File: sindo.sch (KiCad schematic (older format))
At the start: 153 parts, among them J1 Conn_02x06_Odd_Even, J2 Conn_02x06_Odd_Even, U1 ESP32DEVKITV1

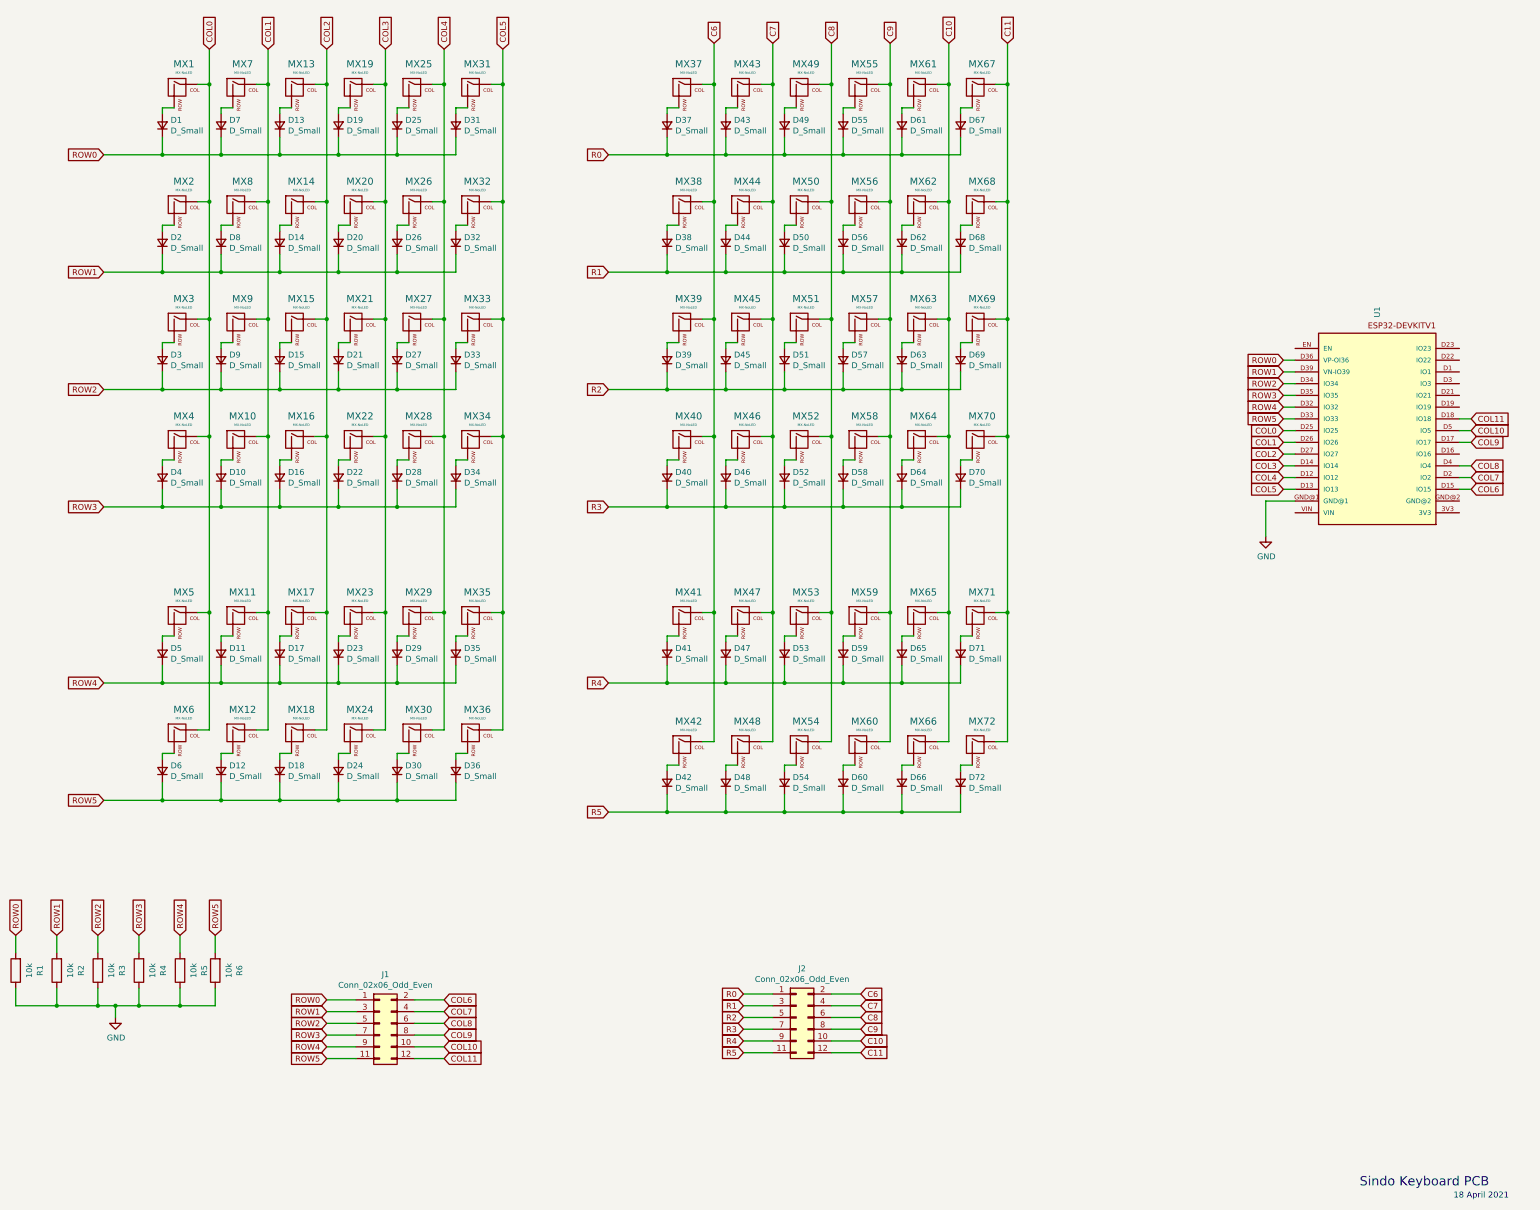
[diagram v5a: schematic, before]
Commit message: Reworked the layout for a single layer
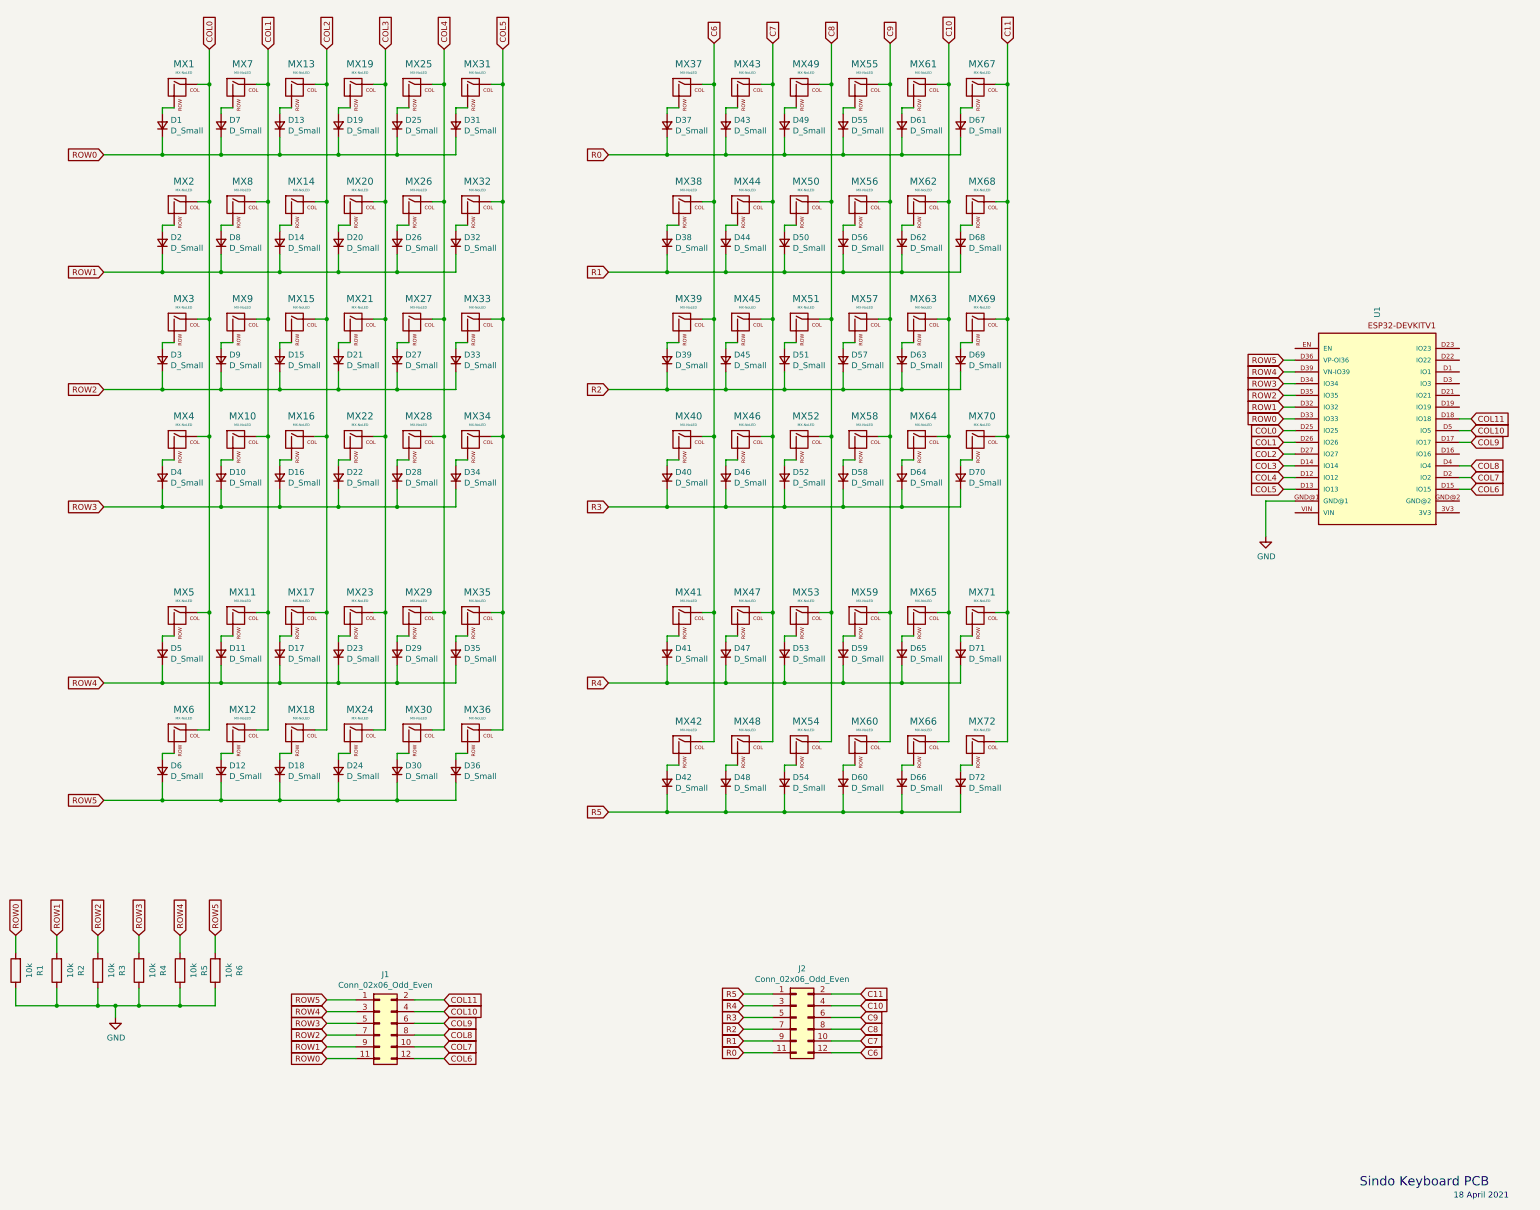
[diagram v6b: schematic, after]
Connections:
- net C10: now also J2.4 (Pin_4); no longer J2.10 (Pin_10)
- net C11: now also J2.2 (Pin_2); no longer J2.12 (Pin_12)
- net C6: now also J2.12 (Pin_12); no longer J2.2 (Pin_2)
- net C7: now also J2.10 (Pin_10); no longer J2.4 (Pin_4)
- net C8: now also J2.8 (Pin_8); no longer J2.6 (Pin_6)
- net C9: now also J2.6 (Pin_6); no longer J2.8 (Pin_8)
- net COL10: now also J1.4 (Pin_4); no longer J1.10 (Pin_10)
- net COL11: now also J1.2 (Pin_2); no longer J1.12 (Pin_12)
- net COL6: now also J1.12 (Pin_12); no longer J1.2 (Pin_2)
- net COL7: now also J1.10 (Pin_10); no longer J1.4 (Pin_4)
- net COL8: now also J1.8 (Pin_8); no longer J1.6 (Pin_6)
- net COL9: now also J1.6 (Pin_6); no longer J1.8 (Pin_8)
- net R0: now also J2.11 (Pin_11); no longer J2.1 (Pin_1)
- net R1: now also J2.9 (Pin_9); no longer J2.3 (Pin_3)
- net R2: now also J2.7 (Pin_7); no longer J2.5 (Pin_5)
- net R3: now also J2.5 (Pin_5); no longer J2.7 (Pin_7)
- net R4: now also J2.3 (Pin_3); no longer J2.9 (Pin_9)
- net R5: now also J2.1 (Pin_1); no longer J2.11 (Pin_11)
- net ROW0: now also J1.11 (Pin_11), U1.D33 (IO33); no longer J1.1 (Pin_1), U1.D36 (VP-OI36)
- net ROW1: now also J1.9 (Pin_9), U1.D32 (IO32); no longer J1.3 (Pin_3), U1.D39 (VN-IO39)
- net ROW2: now also J1.7 (Pin_7), U1.D35 (IO35); no longer J1.5 (Pin_5), U1.D34 (IO34)
- net ROW3: now also J1.5 (Pin_5), U1.D34 (IO34); no longer J1.7 (Pin_7), U1.D35 (IO35)
- net ROW4: now also J1.3 (Pin_3), U1.D39 (VN-IO39); no longer J1.9 (Pin_9), U1.D32 (IO32)
- net ROW5: now also J1.1 (Pin_1), U1.D36 (VP-OI36); no longer J1.11 (Pin_11), U1.D33 (IO33)
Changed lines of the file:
@@
 Text GLabel 4900 1250 1    50   Input ~ 0
 COL5
+Text GLabel 3400 9850 0    50   Input ~ 0
+ROW0
+Text GLabel 3400 9650 0    50   Input ~ 0
+ROW2
+Text GLabel 3400 9550 0    50   Input ~ 0
+ROW3
+Text GLabel 3400 9450 0    50   Input ~ 0
+ROW4
 Text GLabel 3400 9350 0    50   Input ~ 0
-ROW0
-Text GLabel 3400 9450 0    50   Input ~ 0
-ROW1
-Text GLabel 3400 9550 0    50   Input ~ 0
-ROW2
-Text GLabel 3400 9650 0    50   Input ~ 0
-ROW3
-Text GLabel 3400 9750 0    50   Input ~ 0
-ROW4
-Text GLabel 3400 9850 0    50   Input ~ 0
 ROW5
+Text GLabel 4400 9850 2    50   Input ~ 0
+COL6
+Text GLabel 4400 9750 2    50   Input ~ 0
+COL7
+Text GLabel 4400 9650 2    50   Input ~ 0
+COL8
+Text GLabel 4400 9550 2    50   Input ~ 0
+COL9
+Text GLabel 4400 9450 2    50   Input ~ 0
+COL10
 Text GLabel 4400 9350 2    50   Input ~ 0
-COL6
-Text GLabel 4400 9450 2    50   Input ~ 0
-COL7
-Text GLabel 4400 9550 2    50   Input ~ 0
-COL8
-Text GLabel 4400 9650 2    50   Input ~ 0
-COL9
-Text GLabel 4400 9750 2    50   Input ~ 0
-COL10
-Text GLabel 4400 9850 2    50   Input ~ 0
 COL11
 $Comp
@@
 	0    -1   -1   0
 $EndComp
+Text GLabel 11550 3900 0    50   Input ~ 0
+ROW5
+Text GLabel 11550 4000 0    50   Input ~ 0
+ROW4
+Text GLabel 11550 4100 0    50   Input ~ 0
+ROW3
+Text GLabel 11550 4200 0    50   Input ~ 0
+ROW2
+Text GLabel 11550 4300 0    50   Input ~ 0
+ROW1
 Text GLabel 11550 4400 0    50   Input ~ 0
-ROW5
-Text GLabel 11550 4300 0    50   Input ~ 0
-ROW4
-Text GLabel 11550 4200 0    50   Input ~ 0
-ROW3
-Text GLabel 11550 4100 0    50   Input ~ 0
-ROW2
-Text GLabel 11550 4000 0    50   Input ~ 0
-ROW1
-Text GLabel 11550 3900 0    50   Input ~ 0
 ROW0
 Text GLabel 11550 4500 0    50   Input ~ 0
@@
 Wire Wire Line
 	3400 9850 3650 9850
-Text GLabel 6950 9300 0    50   Input ~ 0
-R0
-Text GLabel 6950 9400 0    50   Input ~ 0
-R1
-Text GLabel 6950 9500 0    50   Input ~ 0
-R2
-Text GLabel 6950 9600 0    50   Input ~ 0
-R3
-Text GLabel 6950 9700 0    50   Input ~ 0
-R4
-Text GLabel 6950 9800 0    50   Input ~ 0
-R5
-Text GLabel 7950 9300 2    50   Input ~ 0
-C6
-Text GLabel 7950 9400 2    50   Input ~ 0
-C7
-Text GLabel 7950 9500 2    50   Input ~ 0
-C8
-Text GLabel 7950 9600 2    50   Input ~ 0
-C9
-Text GLabel 7950 9700 2    50   Input ~ 0
-C10
-Text GLabel 7950 9800 2    50   Input ~ 0
-C11
 Wire Wire Line
 	7200 9300 6950 9300
@@
 	1    0    0    -1
 $EndComp
+Text GLabel 3400 9750 0    50   Input ~ 0
+ROW1
+Text GLabel 6950 9300 0    50   Input ~ 0
+R5
+Text GLabel 6950 9800 0    50   Input ~ 0
+R0
+Text GLabel 6950 9700 0    50   Input ~ 0
+R1
+Text GLabel 6950 9400 0    50   Input ~ 0
+R4
+Text GLabel 6950 9500 0    50   Input ~ 0
+R3
+Text GLabel 6950 9600 0    50   Input ~ 0
+R2
+Text GLabel 7950 9300 2    50   Input ~ 0
+C11
+Text GLabel 7950 9800 2    50   Input ~ 0
+C6
+Text GLabel 7950 9400 2    50   Input ~ 0
+C10
+Text GLabel 7950 9700 2    50   Input ~ 0
+C7
+Text GLabel 7950 9600 2    50   Input ~ 0
+C8
+Text GLabel 7950 9500 2    50   Input ~ 0
+C9
 $EndSCHEMATC

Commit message: Added more realistic footprints for the headers and resistors
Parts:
- J1, J2: footprint Connector_PinHeader_1.27mm:PinHeader_2x06_P1.27mm_Vertical -> Connector_PinHeader_2.54mm:PinHeader_2x06_P2.54mm_Vertical
- R1, R2, R3, R4, R5, R6: footprint Resistor_THT:R_Axial_DIN0207_L6.3mm_D2.5mm_P5.08mm_Vertical -> Resistor_THT:R_Axial_DIN0411_L9.9mm_D3.6mm_P7.62mm_Vertical
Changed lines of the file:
@@
 F 0 "R1" V 543 9100 50  0000 C CNN
 F 1 "10k" V 634 9100 50  0000 C CNN
-F 2 "Resistor_THT:R_Axial_DIN0207_L6.3mm_D2.5mm_P5.08mm_Vertical" V 680 9100 50  0001 C CNN
+F 2 "Resistor_THT:R_Axial_DIN0411_L9.9mm_D3.6mm_P7.62mm_Vertical" V 680 9100 50  0001 C CNN
 F 3 "~" H 750 9100 50  0001 C CNN
 	1    750  9100
@@
 F 0 "R2" V 893 9100 50  0000 C CNN
 F 1 "10k" V 984 9100 50  0000 C CNN
-F 2 "Resistor_THT:R_Axial_DIN0207_L6.3mm_D2.5mm_P5.08mm_Vertical" V 1030 9100 50  0001 C CNN
+F 2 "Resistor_THT:R_Axial_DIN0411_L9.9mm_D3.6mm_P7.62mm_Vertical" V 1030 9100 50  0001 C CNN
 F 3 "~" H 1100 9100 50  0001 C CNN
 	1    1100 9100
@@
 F 0 "R3" V 1243 9100 50  0000 C CNN
 F 1 "10k" V 1334 9100 50  0000 C CNN
-F 2 "Resistor_THT:R_Axial_DIN0207_L6.3mm_D2.5mm_P5.08mm_Vertical" V 1380 9100 50  0001 C CNN
+F 2 "Resistor_THT:R_Axial_DIN0411_L9.9mm_D3.6mm_P7.62mm_Vertical" V 1380 9100 50  0001 C CNN
 F 3 "~" H 1450 9100 50  0001 C CNN
 	1    1450 9100
@@
 F 0 "R4" V 1593 9100 50  0000 C CNN
 F 1 "10k" V 1684 9100 50  0000 C CNN
-F 2 "Resistor_THT:R_Axial_DIN0207_L6.3mm_D2.5mm_P5.08mm_Vertical" V 1730 9100 50  0001 C CNN
+F 2 "Resistor_THT:R_Axial_DIN0411_L9.9mm_D3.6mm_P7.62mm_Vertical" V 1730 9100 50  0001 C CNN
 F 3 "~" H 1800 9100 50  0001 C CNN
 	1    1800 9100
@@
 F 0 "R5" V 1943 9100 50  0000 C CNN
 F 1 "10k" V 2034 9100 50  0000 C CNN
-F 2 "Resistor_THT:R_Axial_DIN0207_L6.3mm_D2.5mm_P5.08mm_Vertical" V 2080 9100 50  0001 C CNN
+F 2 "Resistor_THT:R_Axial_DIN0411_L9.9mm_D3.6mm_P7.62mm_Vertical" V 2080 9100 50  0001 C CNN
 F 3 "~" H 2150 9100 50  0001 C CNN
 	1    2150 9100
@@
 F 0 "R6" V 2243 9100 50  0000 C CNN
 F 1 "10k" V 2334 9100 50  0000 C CNN
-F 2 "Resistor_THT:R_Axial_DIN0207_L6.3mm_D2.5mm_P5.08mm_Vertical" V 2380 9100 50  0001 C CNN
+F 2 "Resistor_THT:R_Axial_DIN0411_L9.9mm_D3.6mm_P7.62mm_Vertical" V 2380 9100 50  0001 C CNN
 F 3 "~" H 2450 9100 50  0001 C CNN
 	1    2450 9100
@@
 F 0 "J1" H 3900 9967 50  0000 C CNN
 F 1 "Conn_02x06_Odd_Even" H 3900 9876 50  0000 C CNN
-F 2 "Connector_PinHeader_1.27mm:PinHeader_2x06_P1.27mm_Vertical" H 3850 9550 50  0001 C CNN
+F 2 "Connector_PinHeader_2.54mm:PinHeader_2x06_P2.54mm_Vertical" H 3850 9550 50  0001 C CNN
 F 3 "~" H 3850 9550 50  0001 C CNN
 	1    3850 9550
@@
 F 0 "J2" H 7450 9917 50  0000 C CNN
 F 1 "Conn_02x06_Odd_Even" H 7450 9826 50  0000 C CNN
-F 2 "Connector_PinHeader_1.27mm:PinHeader_2x06_P1.27mm_Vertical" H 7400 9500 50  0001 C CNN
+F 2 "Connector_PinHeader_2.54mm:PinHeader_2x06_P2.54mm_Vertical" H 7400 9500 50  0001 C CNN
 F 3 "~" H 7400 9500 50  0001 C CNN
 	1    7400 9500
